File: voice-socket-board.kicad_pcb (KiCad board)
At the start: 2 copper layers, 150 x 100 mm, 280 parts, among them J1 JACK_MONO_SW, J2 JACK_MONO_SW, J3 JACK_MONO_SW, P1 CONN_01X03, P2 CONN_01X03, P3 CONN_02X05, P4 DDR3-DIMM, Q1 MMBT3904, Q10 2N3906, Q2 DMMT3904W, Q3 2N7002, Q4 2N7002, Q5 MMBT3904, Q6 2N3906, Q7 MMBT3904, Q8 MMBT3904, Q9 MMBT3904, SW1 SPST, SW10 SP3T, SW11 SP3T, SW12 SP3T, SW13 SP3T, SW14 SPST, SW15 TACT_SWITCH, SW2 SPST, SW3 SP3T, SW4 SP3T, SW5 SPST, SW6 SPST, SW7 Switch_SPDT_x2, SW8 2P3T, SW9 SP3T, U1 LM833, U10 TL072-, U11 NE5534, U2 TL072-, U3 TL072-, U4 TL072-, U5 TL072-, U6 TL072-, U7 MAX9945, U8 CD4013, U9 TL072-

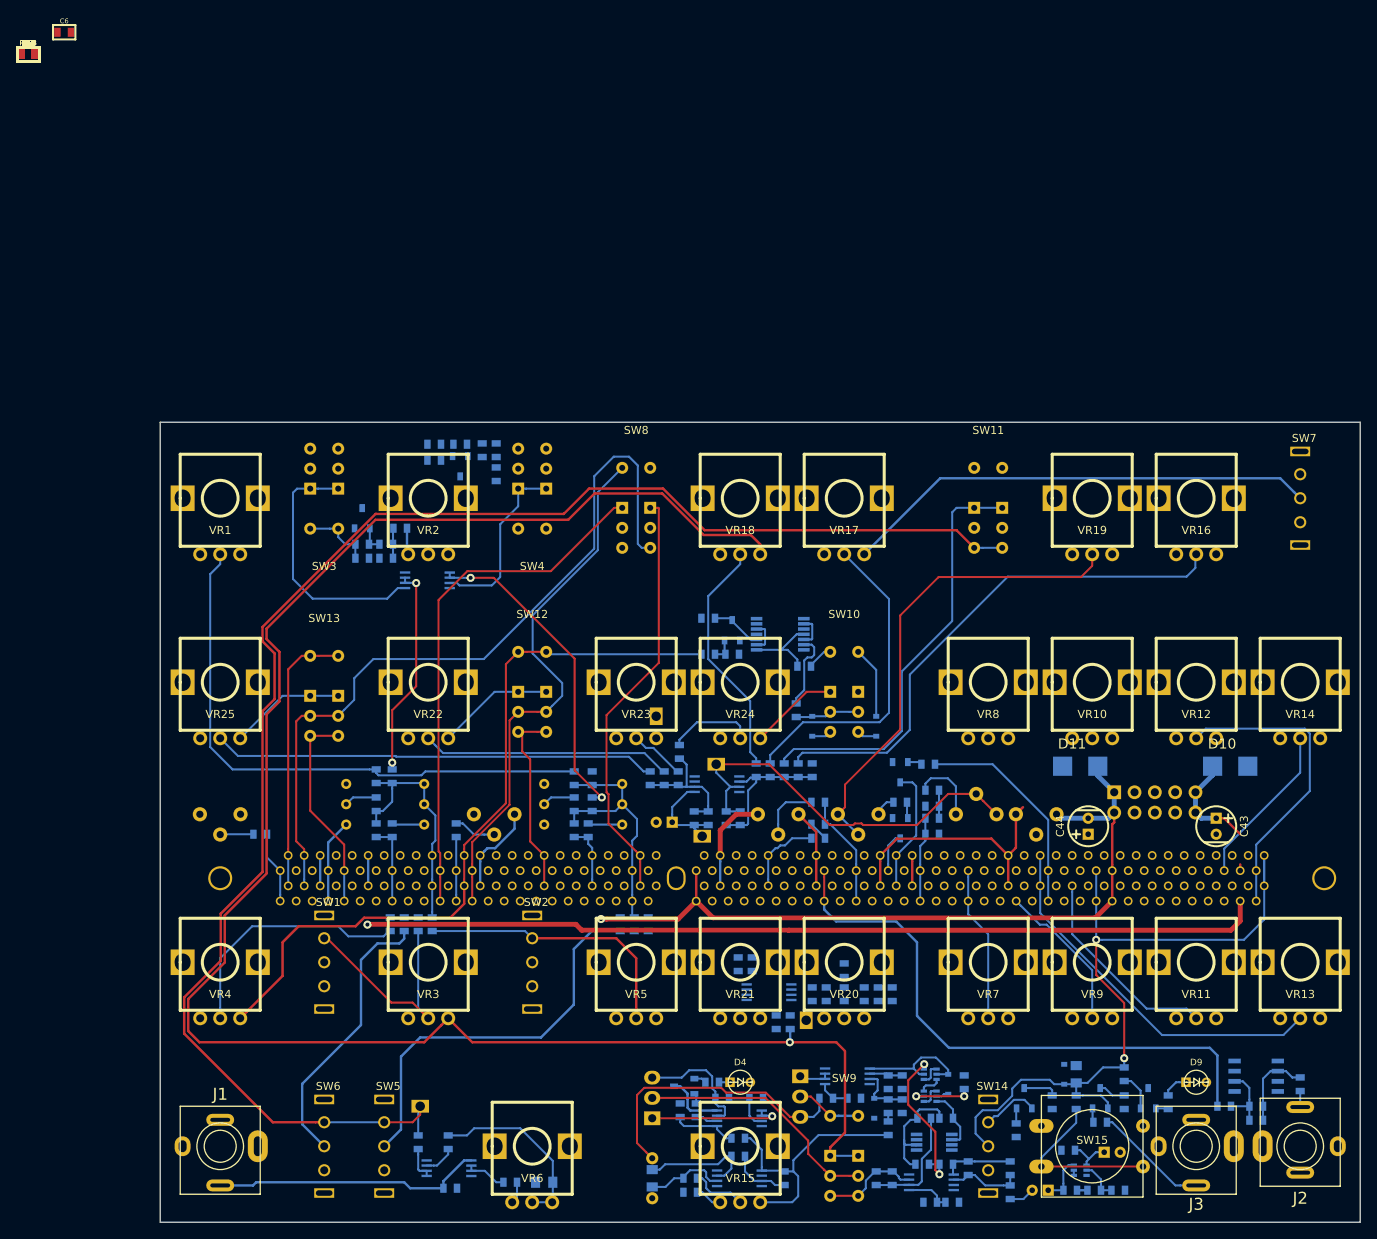
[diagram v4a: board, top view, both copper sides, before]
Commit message: routing. moved power connector
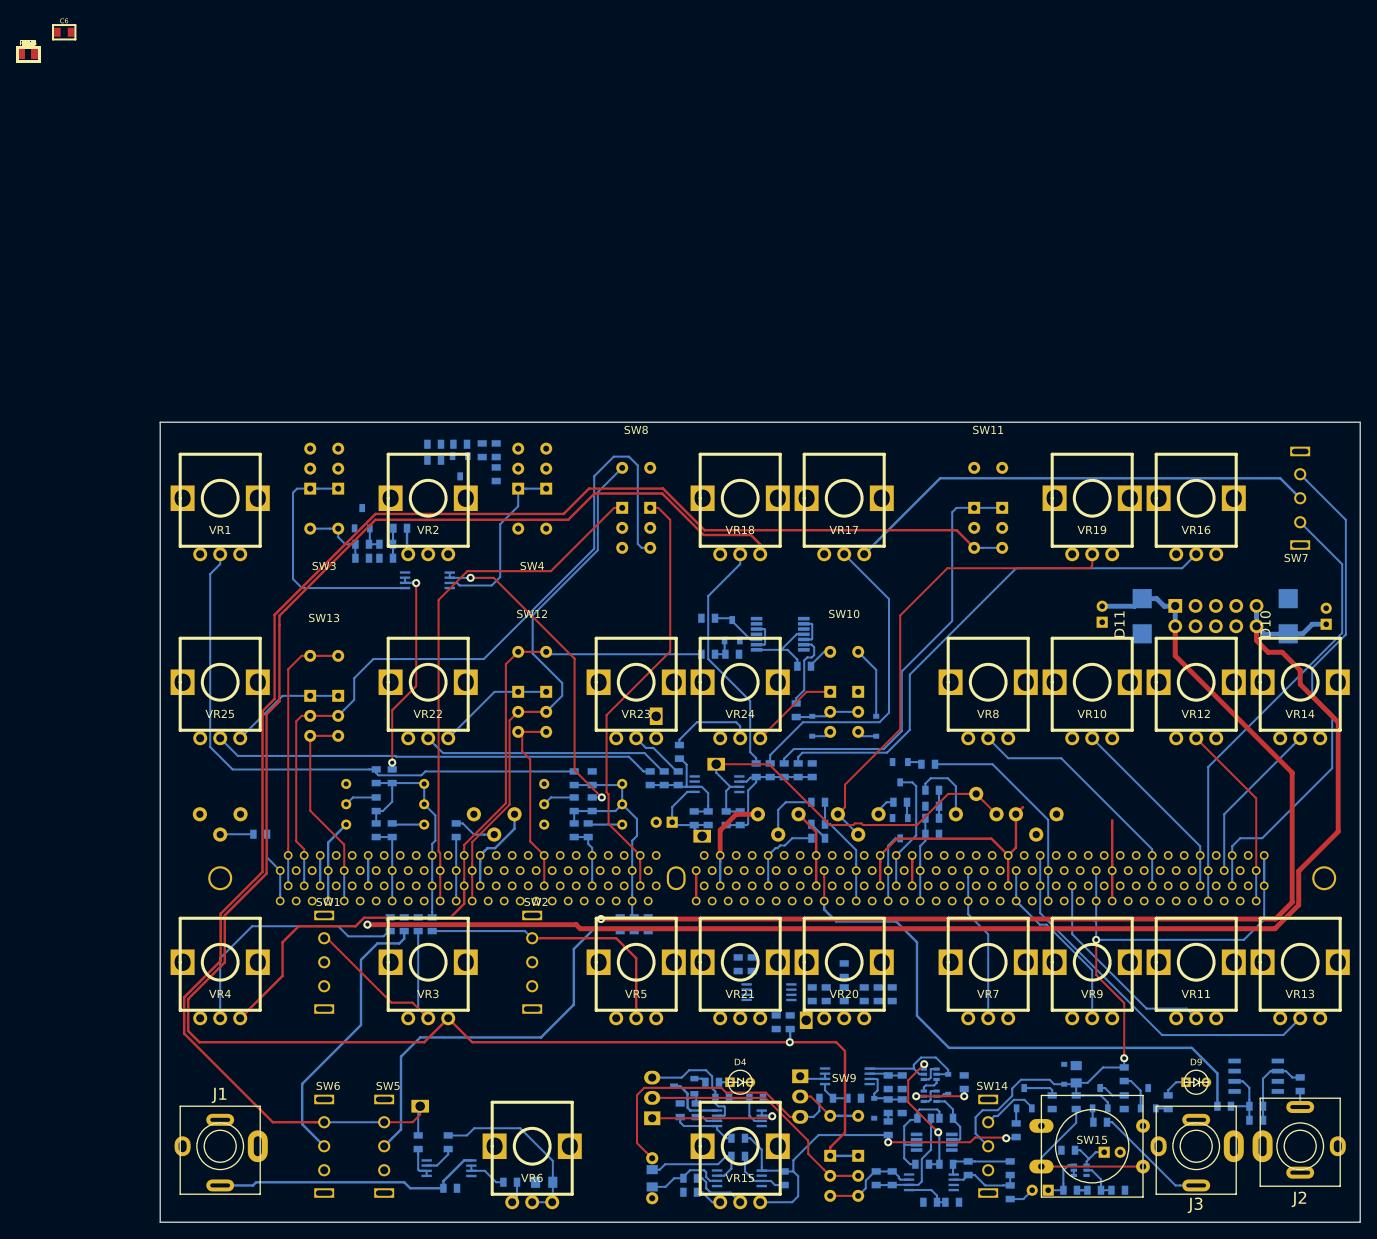
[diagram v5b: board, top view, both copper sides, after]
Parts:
- C43, C44: moved to B.Cu
- moved C43 29.6 mm to (190.8, 64.2), turned to 90 degrees
- moved C44 26.6 mm to (162.8, 64.0)
- moved P3 24.5 mm to (171.9, 63.0)
- moved D11 20.3 mm to (167.8, 64.2), turned to 270 degrees
- moved D10 20.1 mm to (186.0, 64.2), turned to 270 degrees
- turned SW7 to 90 degrees
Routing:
- net EG2_ENV_OUT: track 0.00 -> 63.4 mm
- net -12V: track 123.4 -> 182.4 mm
- net EG2_INV_OUT: track 0.00 -> 56.5 mm
- net +12V: track 199.8 -> 245.9 mm
- net EG2_ATTACK_CV: track 0.00 -> 30.8 mm
- net EG2_DECAY_CV: track 0.00 -> 24.0 mm
- net LFO_GATE: track 32.3 -> 49.5 mm, vias 0 -> 2
- net EG2_SUSTAIN_CV: track 38.7 -> 23.5 mm
- net RES_CTRL: track 5.01 -> 8.81 mm
- net EG1_DECAY_CV: track 19.1 -> 22.9 mm
- net Net-(Q3-Pad6): track 19.4 -> 16.9 mm
- net LFO_OUT: track 232.8 -> 231.5 mm
- net VCA_OUT: track 73.3 -> 72.0 mm
- net KEY_TRACK: track 198.1 -> 196.9 mm
- net VCO2_SYNC_IN: track 52.7 -> 53.9 mm
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
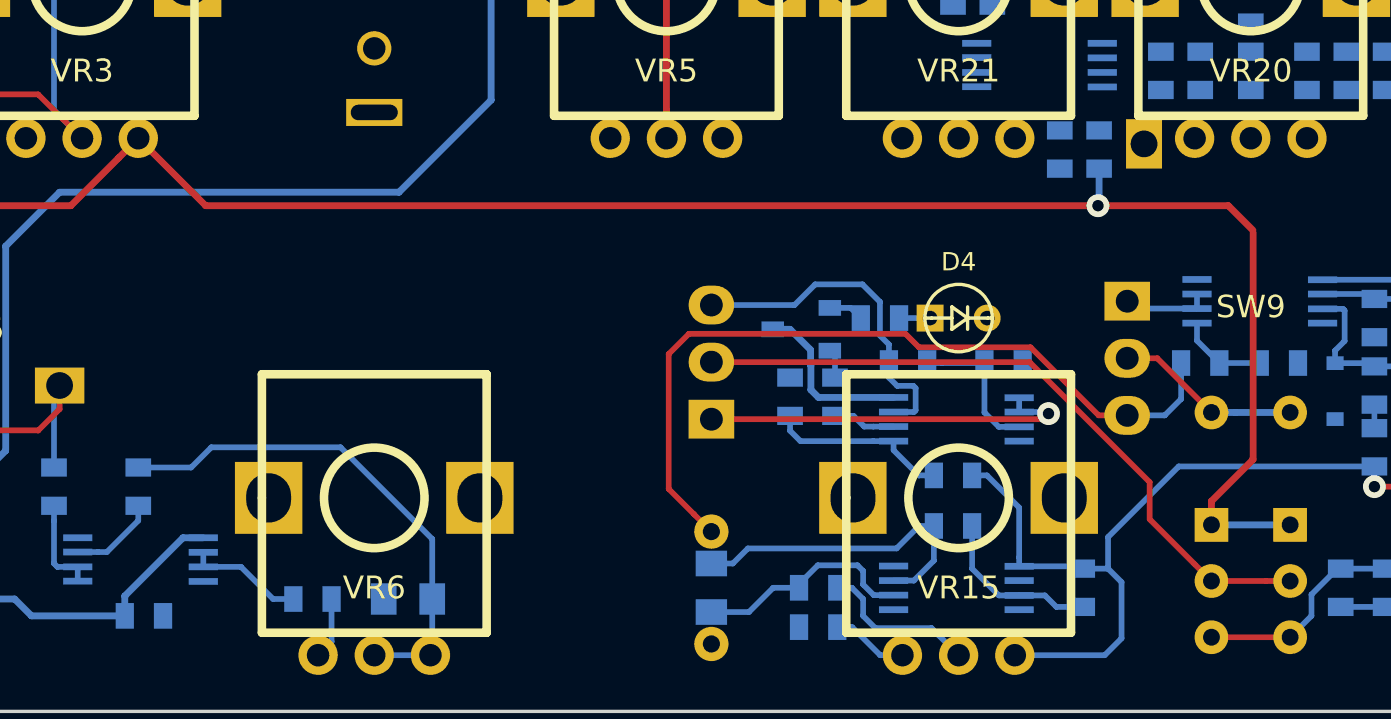
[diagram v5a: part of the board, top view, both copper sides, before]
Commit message: changed around LFO jumpers to reduce via count by one
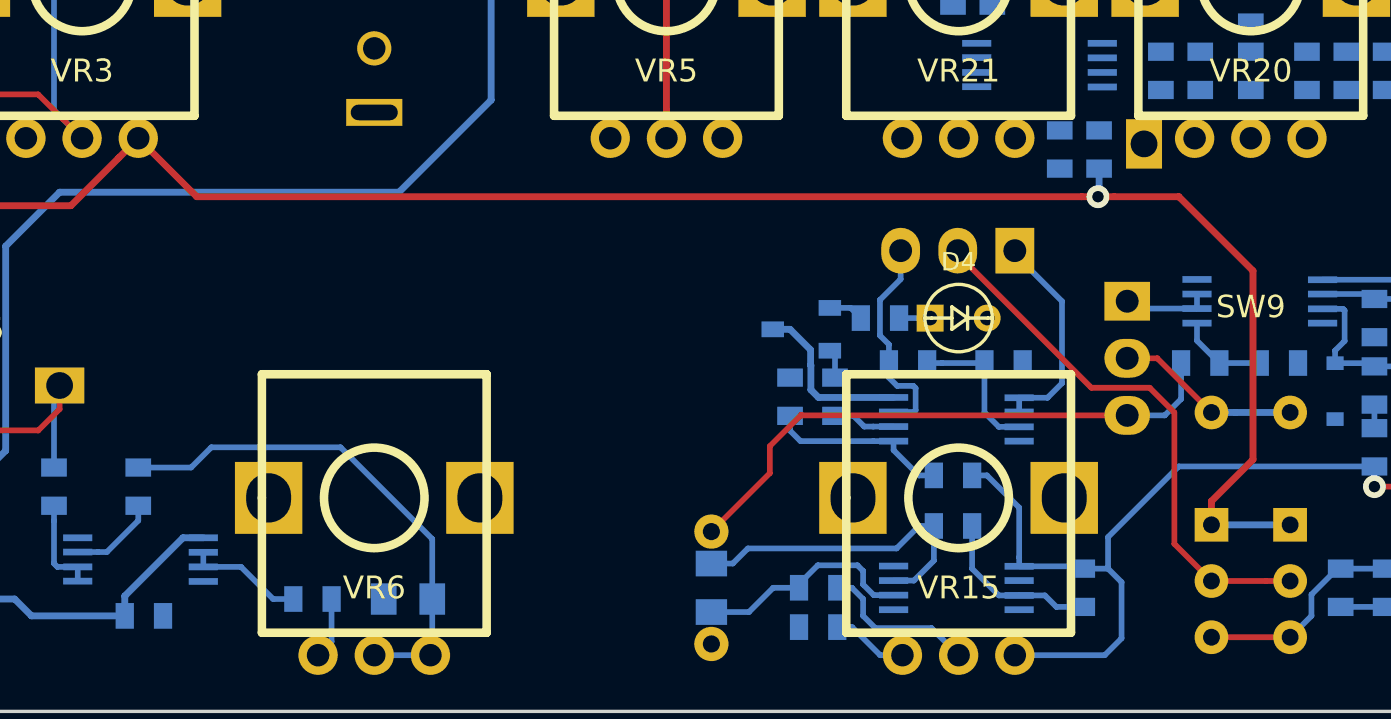
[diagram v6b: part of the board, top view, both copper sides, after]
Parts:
- moved P2 15.4 mm to (120.0, 119.5), turned to 90 degrees
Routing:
- net Net-(C14-Pad2): track 49.6 -> 40.0 mm
- net Net-(P2-Pad1): track 17.1 -> 9.58 mm, vias 1 -> 0
- net LFO_PULSE: track 30.8 -> 24.4 mm
- net Net-(P2-Pad3): track 15.1 -> 9.57 mm
- net LFO_OUT: track 231.5 -> 230.1 mm

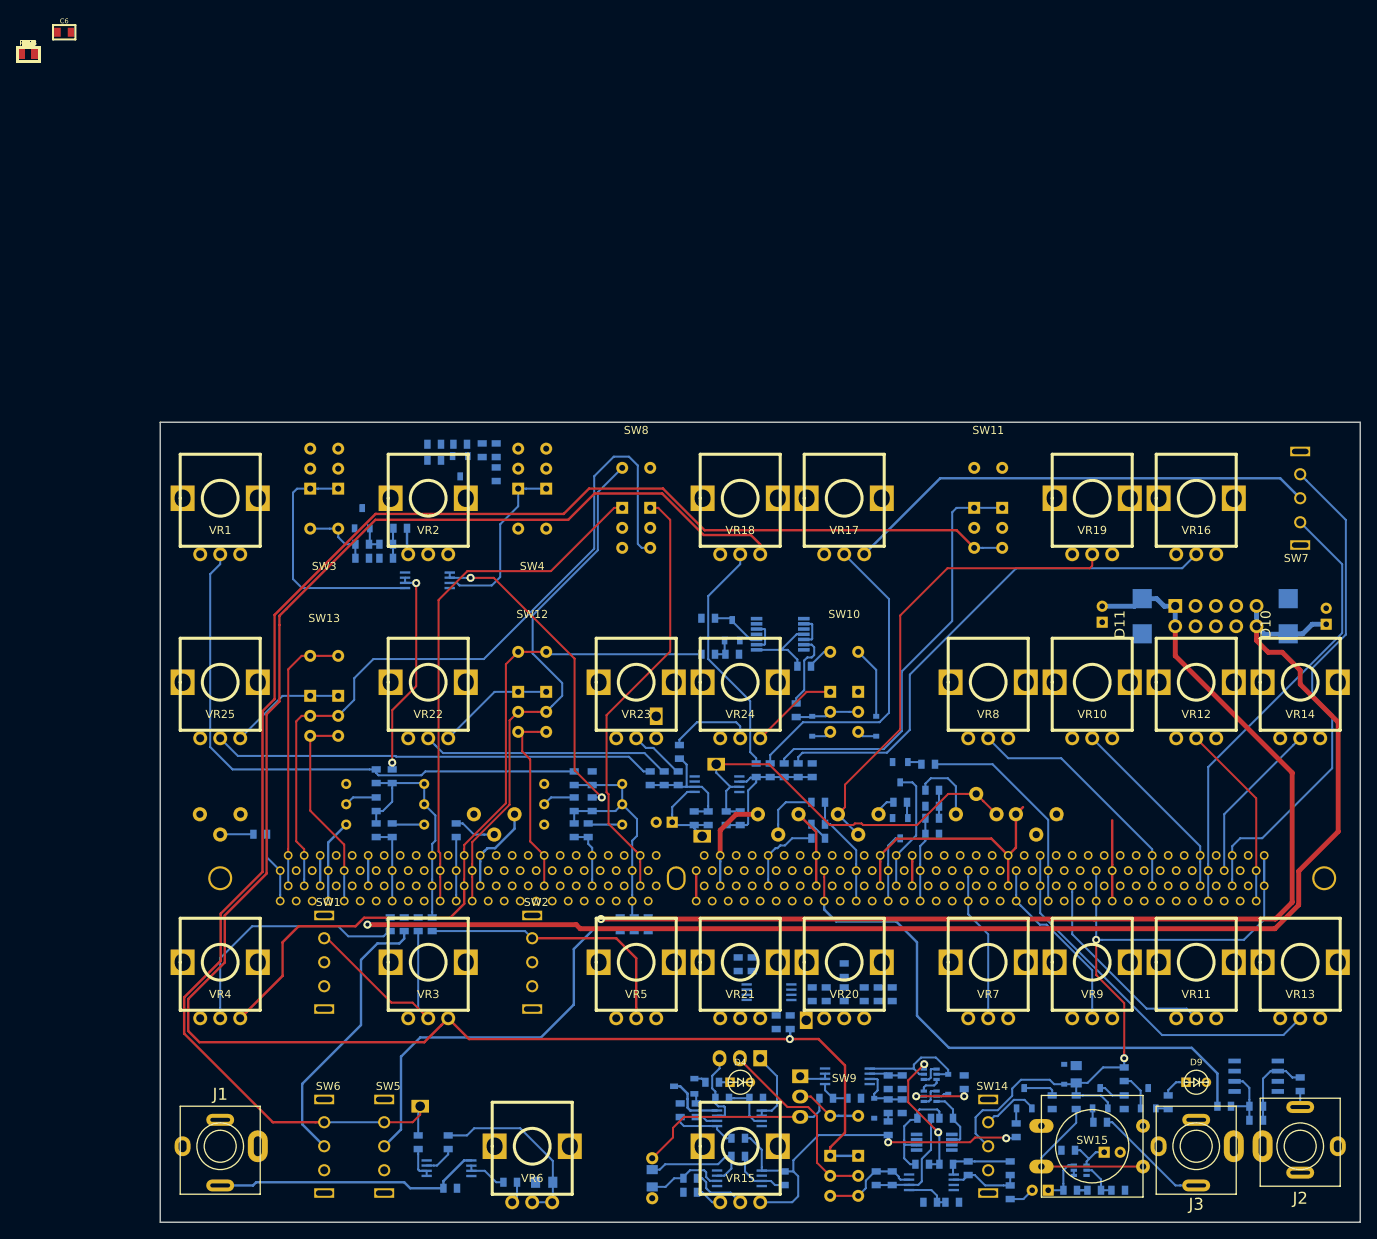
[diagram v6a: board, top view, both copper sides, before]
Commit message: added top and bottom ground planes
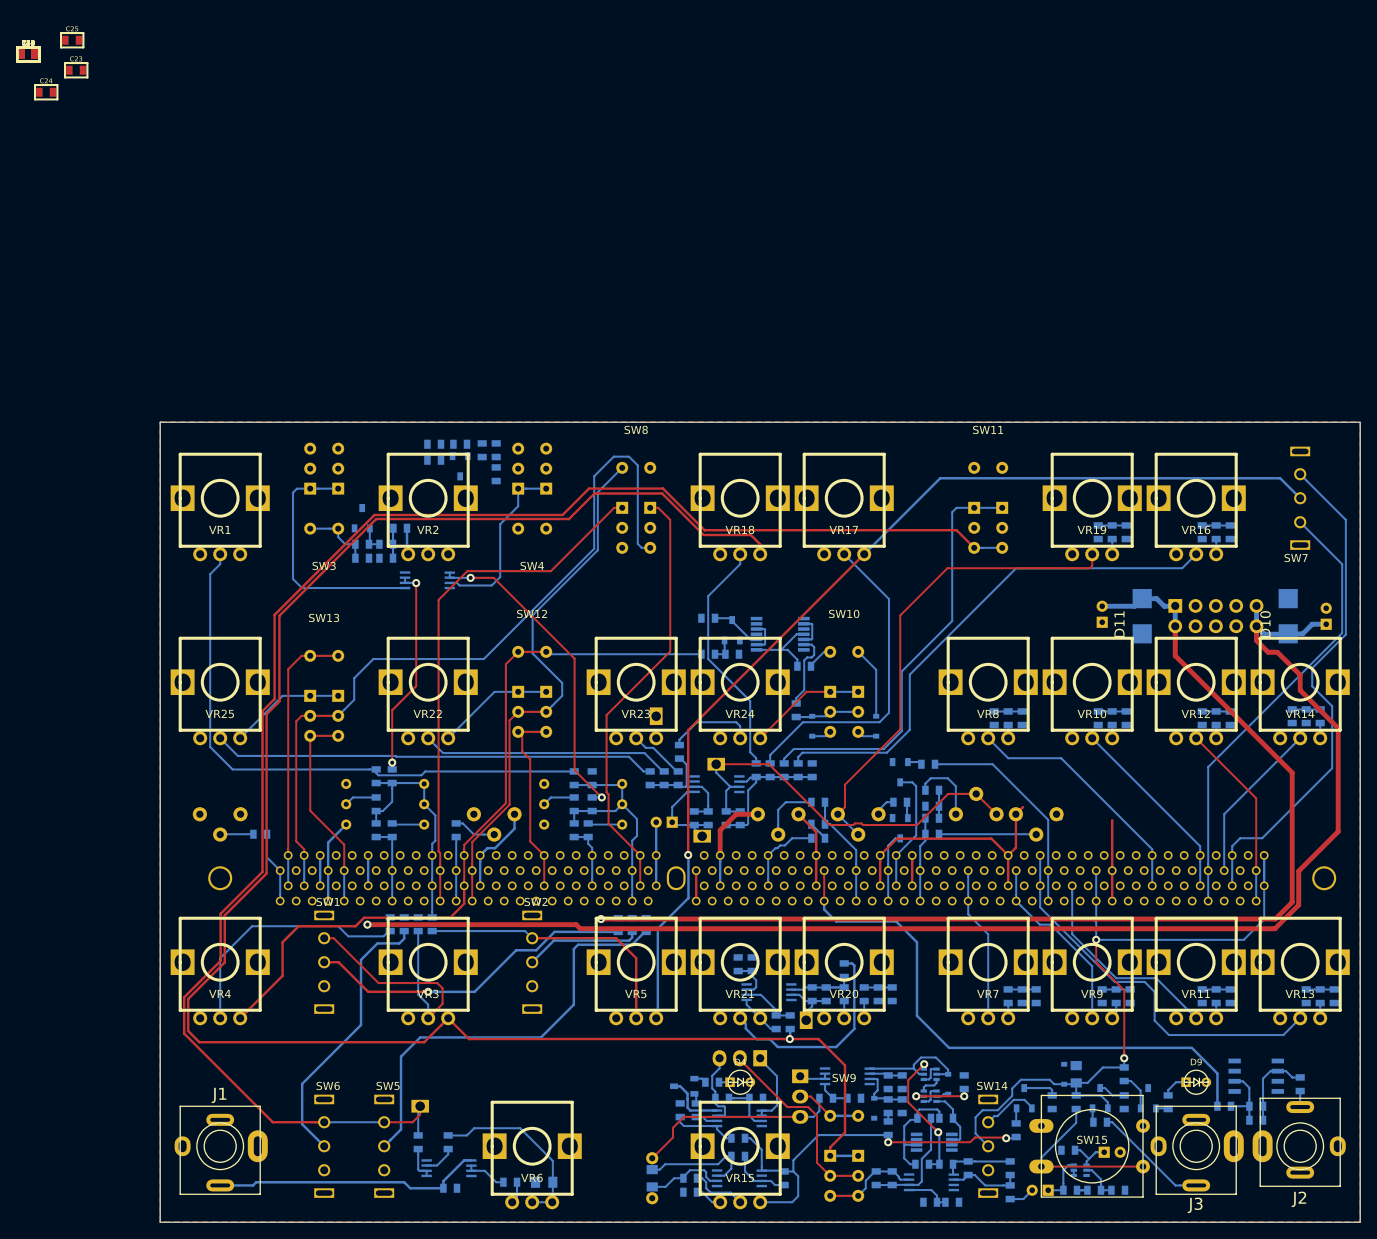
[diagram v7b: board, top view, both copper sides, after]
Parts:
- C10, C11, C12, C13, C55, C56, C6, C7, C8, C9, R103, R104, R32, R33, R34, R35, R36, R37, R38, R39, R40, R41, R42, R43, R44, R45, R46, R47, R95, R96: moved to B.Cu
- moved R44 201.3 mm to (191.8, 111.8), turned to 90 degrees
- moved R45 199.9 mm to (190.0, 111.8), turned to 270 degrees
- moved C12 198.5 mm to (188.2, 111.8), turned to 270 degrees
- moved R40 190.9 mm to (178.8, 111.8), turned to 90 degrees
- moved R41 189.5 mm to (177.0, 111.8), turned to 270 degrees
- moved C10 188.1 mm to (175.2, 111.8), turned to 270 degrees
- moved R47 181.5 mm to (190.0, 76.8), turned to 270 degrees
- moved R36 181.2 mm to (166.2, 111.8), turned to 90 degrees
- moved C13 179.9 mm to (188.2, 76.8), turned to 270 degrees
- moved R37 179.9 mm to (164.5, 111.8), turned to 270 degrees
- moved C8 178.6 mm to (162.8, 111.8), turned to 270 degrees
- moved R46 178.4 mm to (186.5, 76.8), turned to 90 degrees
- moved R32 172.5 mm to (154.5, 111.8), turned to 90 degrees
- moved R42 171.6 mm to (178.8, 77.0), turned to 90 degrees
- moved R43 170.1 mm to (177.0, 77.0), turned to 270 degrees
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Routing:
- net EG2_OUT: track 59.5 -> 128.3 mm, vias 0 -> 1
- net Net-(R10-Pad2): track 0.00 -> 41.4 mm, vias 0 -> 1
- net Net-(R90-Pad2): track 0.00 -> 26.3 mm
- net Net-(R11-Pad2): track 0.00 -> 14.5 mm
- net Net-(R107-Pad2): track 0.06 -> 12.2 mm
- net Net-(C54-Pad1): track 0.00 -> 8.02 mm
- net VCF_IN: track 0.00 -> 7.95 mm
- net VCO1_PWM_CV: track 0.00 -> 7.39 mm
- net Net-(R85-Pad1): track 0.00 -> 6.90 mm
- net VCO2_GLIDE_CV: track 46.5 -> 53.3 mm
- net VCO2_PITCH_CV: track 35.3 -> 29.6 mm
- net Net-(R89-Pad1): track 0.00 -> 5.56 mm
- net Net-(R84-Pad2): track 0.00 -> 5.29 mm
- net LFO_MOD: track 28.6 -> 33.3 mm
- net SUB_OSC: track 11.2 -> 14.7 mm
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- added copper zone on B.Cu, net GND
- added copper zone on F.Cu, net GND
